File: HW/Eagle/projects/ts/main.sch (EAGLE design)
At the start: 46 parts, among them IC1 4050D, T1 IRFZ24N, T2 IRFZ24N, U1 ATMEGA328P-PU, U2 LM2576T, U3 HT7533, U4 LM75

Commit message: Minor HW changes
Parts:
- added H1: MOUNT-PAD-ROUND3.6, holes:MOUNT-PAD-ROUND3.6
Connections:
- net GND: now also H1.MOUNT
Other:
- moved on the sheet: LED1, R4, R9
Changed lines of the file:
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@@
 <part name="R13" library="rcl" deviceset="R-EU_" device="R0805" value="330R"/>
 <part name="LED1" library="led" deviceset="LED" device="5MM"/>
+<part name="H1" library="holes" deviceset="MOUNT-PAD-ROUND" device="3.6"/>
+<part name="GND11" library="supply1" deviceset="GND" device=""/>
 </parts>
 <sheets>
@@
 <instance part="+3V4" gate="G$1" x="246.888" y="88.9" rot="MR0"/>
 <instance part="GND13" gate="1" x="246.888" y="68.58" rot="MR0"/>
-<instance part="R4" gate="G$1" x="124.46" y="27.94"/>
+<instance part="R4" gate="G$1" x="134.62" y="27.94"/>
 <instance part="RESET" gate="1" x="220.98" y="114.3" rot="R270"/>
 <instance part="GND14" gate="1" x="213.36" y="106.68"/>
@@
 <instance part="R8" gate="G$1" x="21.336" y="35.56" rot="R180"/>
 <instance part="KEYPAD" gate="1" x="60.96" y="152.4"/>
-<instance part="R9" gate="G$1" x="104.14" y="15.24"/>
-<instance part="P+8" gate="VCC" x="97.79" y="19.05"/>
+<instance part="R9" gate="G$1" x="114.3" y="15.24"/>
+<instance part="P+8" gate="VCC" x="107.95" y="19.05"/>
 <instance part="T1" gate="G$1" x="38.1" y="124.46"/>
 <instance part="T2" gate="G$1" x="38.1" y="104.14"/>
@@
 <instance part="R12" gate="G$1" x="20.828" y="101.6" rot="R180"/>
 <instance part="R13" gate="G$1" x="20.828" y="121.92" rot="R180"/>
-<instance part="LED1" gate="G$1" x="114.3" y="15.24" rot="R90"/>
+<instance part="LED1" gate="G$1" x="124.46" y="15.24" rot="R90"/>
+<instance part="H1" gate="G$1" x="33.02" y="63.5"/>
+<instance part="GND11" gate="1" x="27.94" y="58.42"/>
 </instances>
 <busses>
@@
 <junction x="30.48" y="111.252"/>
 </segment>
+<segment>
+<pinref part="H1" gate="G$1" pin="MOUNT"/>
+<pinref part="GND11" gate="1" pin="GND"/>
+<wire x1="30.48" y1="63.5" x2="27.94" y2="63.5" width="0.1524" layer="91"/>
+<wire x1="27.94" y1="63.5" x2="27.94" y2="60.96" width="0.1524" layer="91"/>
+</segment>
 </net>
 <net name="VCC" class="0">
@@
 <pinref part="R9" gate="G$1" pin="1"/>
 <pinref part="P+8" gate="VCC" pin="VCC"/>
-<wire x1="99.06" y1="15.24" x2="97.79" y2="15.24" width="0.1524" layer="91"/>
-<wire x1="97.79" y1="15.24" x2="97.79" y2="16.51" width="0.1524" layer="91"/>
+<wire x1="109.22" y1="15.24" x2="107.95" y2="15.24" width="0.1524" layer="91"/>
+<wire x1="107.95" y1="15.24" x2="107.95" y2="16.51" width="0.1524" layer="91"/>
 </segment>
 </net>
@@
 <segment>
 <pinref part="R4" gate="G$1" pin="2"/>
-<wire x1="129.54" y1="27.94" x2="132.08" y2="27.94" width="0.1524" layer="91"/>
-<label x="132.08" y="27.94" size="1.778" layer="95" xref="yes"/>
+<wire x1="139.7" y1="27.94" x2="142.24" y2="27.94" width="0.1524" layer="91"/>
+<label x="142.24" y="27.94" size="1.778" layer="95" xref="yes"/>
 </segment>
 </net>
@@
 <segment>
 <pinref part="R4" gate="G$1" pin="1"/>
-<wire x1="119.38" y1="27.94" x2="116.84" y2="27.94" width="0.1524" layer="91"/>
-<label x="116.84" y="27.94" size="1.778" layer="95" rot="R180" xref="yes"/>
+<wire x1="129.54" y1="27.94" x2="127" y2="27.94" width="0.1524" layer="91"/>
+<label x="127" y="27.94" size="1.778" layer="95" rot="R180" xref="yes"/>
 </segment>
 <segment>
@@
 <net name="LED" class="0">
 <segment>
-<wire x1="119.38" y1="15.24" x2="124.46" y2="15.24" width="0.1524" layer="91"/>
-<label x="124.46" y="15.24" size="1.778" layer="95" xref="yes"/>
+<wire x1="129.54" y1="15.24" x2="134.62" y2="15.24" width="0.1524" layer="91"/>
+<label x="134.62" y="15.24" size="1.778" layer="95" xref="yes"/>
 <pinref part="LED1" gate="G$1" pin="C"/>
 </segment>
@@
 <segment>
 <pinref part="R9" gate="G$1" pin="2"/>
-<wire x1="109.22" y1="15.24" x2="111.76" y2="15.24" width="0.1524" layer="91"/>
+<wire x1="119.38" y1="15.24" x2="121.92" y2="15.24" width="0.1524" layer="91"/>
 <pinref part="LED1" gate="G$1" pin="A"/>
 </segment>

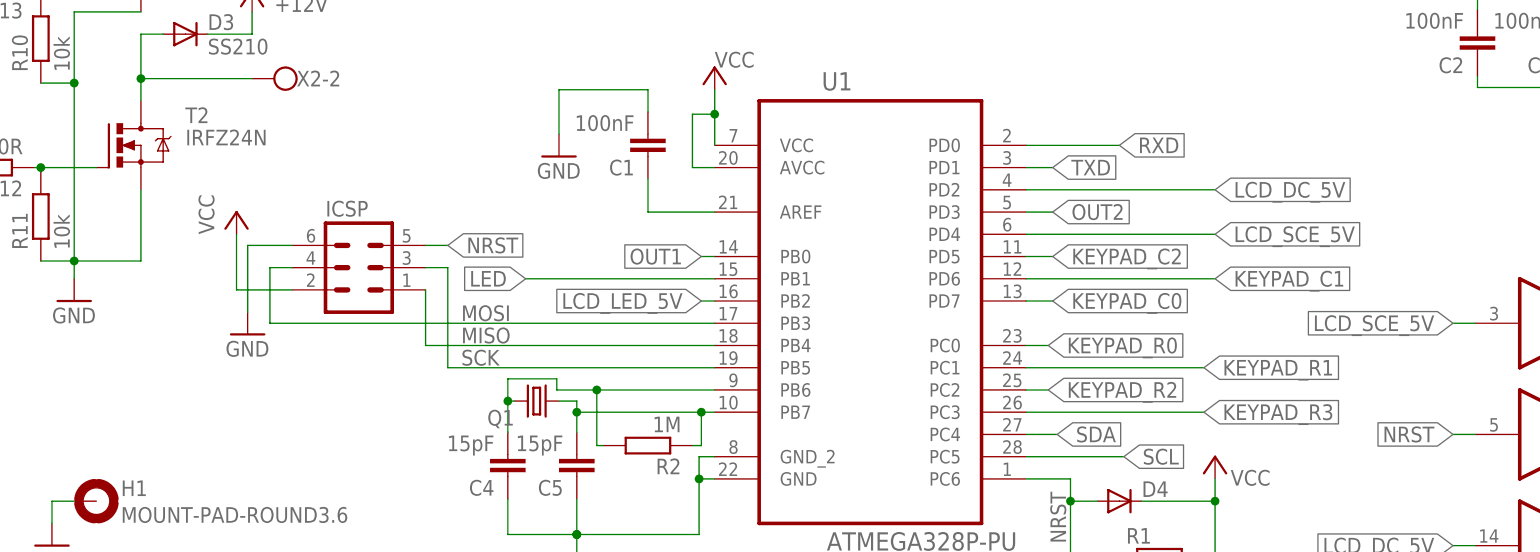
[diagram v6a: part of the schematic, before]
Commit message: Timer 1 is no longer used for PWM
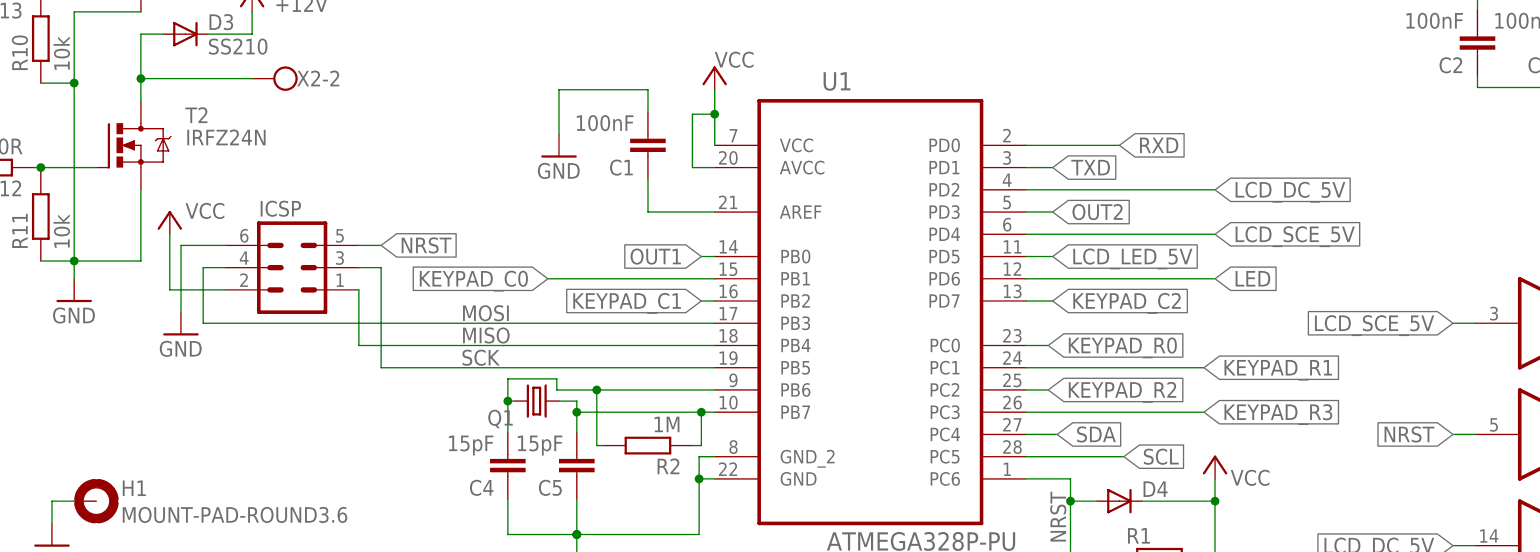
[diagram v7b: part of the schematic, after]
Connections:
- net KEYPAD_C0: now also U1.PB1; no longer U1.PD7
- net KEYPAD_C1: now also U1.PB2; no longer U1.PD6
- net KEYPAD_C2: now also U1.PD7; no longer U1.PD5
- net LCD_LED_5V: now also U1.PD5; no longer U1.PB2
- net LED: now also U1.PD6; no longer U1.PB1
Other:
- moved on the sheet: ICSP
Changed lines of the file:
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@@
 <instance part="R1" gate="G$1" x="154.432" y="57.15"/>
 <instance part="R2" gate="G$1" x="96.012" y="69.85" rot="R180"/>
-<instance part="ICSP" gate="1" x="62.992" y="90.17"/>
-<instance part="P+4" gate="VCC" x="49.022" y="96.52"/>
-<instance part="GND4" gate="1" x="50.292" y="82.55"/>
+<instance part="ICSP" gate="1" x="55.372" y="90.17"/>
+<instance part="P+4" gate="VCC" x="41.402" y="96.52" smashed="yes">
+<attribute name="VALUE" x="43.18" y="95.758" size="1.778" layer="96"/>
+</instance>
+<instance part="GND4" gate="1" x="42.672" y="82.55"/>
 <instance part="U2" gate="U" x="210.82" y="154.94"/>
 <instance part="FRAME1" gate="G$1" x="0" y="0"/>
@@
 <pinref part="ICSP" gate="1" pin="6"/>
 <pinref part="GND4" gate="1" pin="GND"/>
-<wire x1="55.372" y1="92.71" x2="50.292" y2="92.71" width="0.1524" layer="91"/>
-<wire x1="50.292" y1="92.71" x2="50.292" y2="85.09" width="0.1524" layer="91"/>
+<wire x1="47.752" y1="92.71" x2="42.672" y2="92.71" width="0.1524" layer="91"/>
+<wire x1="42.672" y1="92.71" x2="42.672" y2="85.09" width="0.1524" layer="91"/>
 </segment>
 <segment>
@@
 <pinref part="ICSP" gate="1" pin="2"/>
 <pinref part="P+4" gate="VCC" pin="VCC"/>
-<wire x1="55.372" y1="87.63" x2="49.022" y2="87.63" width="0.1524" layer="91"/>
-<wire x1="49.022" y1="87.63" x2="49.022" y2="93.98" width="0.1524" layer="91"/>
+<wire x1="47.752" y1="87.63" x2="41.402" y2="87.63" width="0.1524" layer="91"/>
+<wire x1="41.402" y1="87.63" x2="41.402" y2="93.98" width="0.1524" layer="91"/>
 </segment>
 <segment>
@@
 <segment>
 <pinref part="ICSP" gate="1" pin="1"/>
-<wire x1="103.632" y1="81.28" x2="70.612" y2="81.28" width="0.1524" layer="91"/>
-<wire x1="70.612" y1="81.28" x2="70.612" y2="87.63" width="0.1524" layer="91"/>
+<wire x1="103.632" y1="81.28" x2="62.992" y2="81.28" width="0.1524" layer="91"/>
+<wire x1="62.992" y1="81.28" x2="62.992" y2="87.63" width="0.1524" layer="91"/>
 <pinref part="U1" gate="A" pin="PB4"/>
 <label x="74.676" y="81.534" size="1.778" layer="95"/>
@@
 <segment>
 <pinref part="ICSP" gate="1" pin="5"/>
-<wire x1="70.612" y1="92.71" x2="73.152" y2="92.71" width="0.1524" layer="91"/>
-<label x="73.152" y="92.71" size="1.778" layer="95" xref="yes"/>
+<wire x1="62.992" y1="92.71" x2="65.532" y2="92.71" width="0.1524" layer="91"/>
+<label x="65.532" y="92.71" size="1.778" layer="95" xref="yes"/>
 </segment>
 <segment>
@@
 <segment>
 <pinref part="ICSP" gate="1" pin="4"/>
-<wire x1="52.832" y1="83.82" x2="52.832" y2="90.17" width="0.1524" layer="91"/>
-<wire x1="52.832" y1="90.17" x2="55.372" y2="90.17" width="0.1524" layer="91"/>
+<wire x1="45.212" y1="83.82" x2="45.212" y2="90.17" width="0.1524" layer="91"/>
+<wire x1="45.212" y1="90.17" x2="47.752" y2="90.17" width="0.1524" layer="91"/>
 <pinref part="U1" gate="A" pin="PB3"/>
-<wire x1="103.632" y1="83.82" x2="52.832" y2="83.82" width="0.1524" layer="91"/>
+<wire x1="103.632" y1="83.82" x2="45.212" y2="83.82" width="0.1524" layer="91"/>
 <label x="74.676" y="84.074" size="1.778" layer="95"/>
 </segment>
@@
 <net name="SCK" class="0">
 <segment>
-<wire x1="73.152" y1="78.74" x2="73.152" y2="90.17" width="0.1524" layer="91"/>
+<wire x1="65.532" y1="78.74" x2="65.532" y2="90.17" width="0.1524" layer="91"/>
 <pinref part="ICSP" gate="1" pin="3"/>
-<wire x1="73.152" y1="90.17" x2="70.612" y2="90.17" width="0.1524" layer="91"/>
+<wire x1="65.532" y1="90.17" x2="62.992" y2="90.17" width="0.1524" layer="91"/>
 <pinref part="U1" gate="A" pin="PB5"/>
-<wire x1="103.632" y1="78.74" x2="73.152" y2="78.74" width="0.1524" layer="91"/>
+<wire x1="103.632" y1="78.74" x2="65.532" y2="78.74" width="0.1524" layer="91"/>
 <label x="74.676" y="78.994" size="1.778" layer="95"/>
 </segment>
@@
 </segment>
 <segment>
-<pinref part="U1" gate="A" pin="PB2"/>
-<wire x1="103.632" y1="86.36" x2="102.108" y2="86.36" width="0.1524" layer="91"/>
-<label x="102.108" y="86.36" size="1.778" layer="95" rot="R180" xref="yes"/>
+<pinref part="U1" gate="A" pin="PD5"/>
+<wire x1="139.192" y1="91.44" x2="142.24" y2="91.44" width="0.1524" layer="91"/>
+<label x="142.24" y="91.44" size="1.778" layer="95" xref="yes"/>
 </segment>
 </net>
@@
 </segment>
 <segment>
-<pinref part="U1" gate="A" pin="PD5"/>
-<wire x1="139.192" y1="91.44" x2="142.24" y2="91.44" width="0.1524" layer="91"/>
-<label x="142.24" y="91.44" size="1.778" layer="95" xref="yes"/>
+<pinref part="U1" gate="A" pin="PD7"/>
+<wire x1="139.192" y1="86.36" x2="142.24" y2="86.36" width="0.1524" layer="91"/>
+<label x="142.24" y="86.36" size="1.778" layer="95" xref="yes"/>
 </segment>
 </net>
@@
 </segment>
 <segment>
+<pinref part="U1" gate="A" pin="PB2"/>
+<wire x1="103.632" y1="86.36" x2="102.108" y2="86.36" width="0.1524" layer="91"/>
+<label x="102.108" y="86.36" size="1.778" layer="95" rot="R180" xref="yes"/>
+</segment>
+</net>
+<net name="KEYPAD_C0" class="0">
+<segment>
+<pinref part="KEYPAD" gate="1" pin="1"/>
+<wire x1="68.58" y1="144.78" x2="88.9" y2="144.78" width="0.1524" layer="91"/>
+<label x="88.9" y="144.78" size="1.778" layer="95" xref="yes"/>
+</segment>
+<segment>
+<pinref part="U1" gate="A" pin="PB1"/>
+<wire x1="103.632" y1="88.9" x2="84.582" y2="88.9" width="0.1524" layer="91"/>
+<label x="84.582" y="88.9" size="1.778" layer="95" rot="R180" xref="yes"/>
+</segment>
+</net>
+<net name="OUT2" class="0">
+<segment>
+<pinref part="R12" gate="G$1" pin="2"/>
+<wire x1="15.748" y1="101.6" x2="14.732" y2="101.6" width="0.1524" layer="91"/>
+<label x="14.732" y="101.6" size="1.778" layer="95" rot="R180" xref="yes"/>
+</segment>
+<segment>
+<pinref part="U1" gate="A" pin="PD3"/>
+<wire x1="139.192" y1="96.52" x2="142.24" y2="96.52" width="0.1524" layer="91"/>
+<label x="142.24" y="96.52" size="1.778" layer="95" xref="yes"/>
+</segment>
+</net>
+<net name="LED" class="0">
+<segment>
+<wire x1="129.54" y1="15.24" x2="134.62" y2="15.24" width="0.1524" layer="91"/>
+<label x="134.62" y="15.24" size="1.778" layer="95" xref="yes"/>
+<pinref part="LED1" gate="G$1" pin="C"/>
+</segment>
+<segment>
 <pinref part="U1" gate="A" pin="PD6"/>
 <wire x1="139.192" y1="88.9" x2="160.782" y2="88.9" width="0.1524" layer="91"/>
@@
 </segment>
 </net>
-<net name="KEYPAD_C0" class="0">
-<segment>
-<pinref part="KEYPAD" gate="1" pin="1"/>
-<wire x1="68.58" y1="144.78" x2="88.9" y2="144.78" width="0.1524" layer="91"/>
-<label x="88.9" y="144.78" size="1.778" layer="95" xref="yes"/>
-</segment>
-<segment>
-<pinref part="U1" gate="A" pin="PD7"/>
-<wire x1="139.192" y1="86.36" x2="142.24" y2="86.36" width="0.1524" layer="91"/>
-<label x="142.24" y="86.36" size="1.778" layer="95" xref="yes"/>
-</segment>
-</net>
-<net name="OUT2" class="0">
-<segment>
-<pinref part="R12" gate="G$1" pin="2"/>
-<wire x1="15.748" y1="101.6" x2="14.732" y2="101.6" width="0.1524" layer="91"/>
-<label x="14.732" y="101.6" size="1.778" layer="95" rot="R180" xref="yes"/>
-</segment>
-<segment>
-<pinref part="U1" gate="A" pin="PD3"/>
-<wire x1="139.192" y1="96.52" x2="142.24" y2="96.52" width="0.1524" layer="91"/>
-<label x="142.24" y="96.52" size="1.778" layer="95" xref="yes"/>
-</segment>
-</net>
-<net name="LED" class="0">
-<segment>
-<wire x1="129.54" y1="15.24" x2="134.62" y2="15.24" width="0.1524" layer="91"/>
-<label x="134.62" y="15.24" size="1.778" layer="95" xref="yes"/>
-<pinref part="LED1" gate="G$1" pin="C"/>
-</segment>
-<segment>
-<pinref part="U1" gate="A" pin="PB1"/>
-<wire x1="103.632" y1="88.9" x2="82.042" y2="88.9" width="0.1524" layer="91"/>
-<label x="82.042" y="88.9" size="1.778" layer="95" rot="R180" xref="yes"/>
-</segment>
-</net>

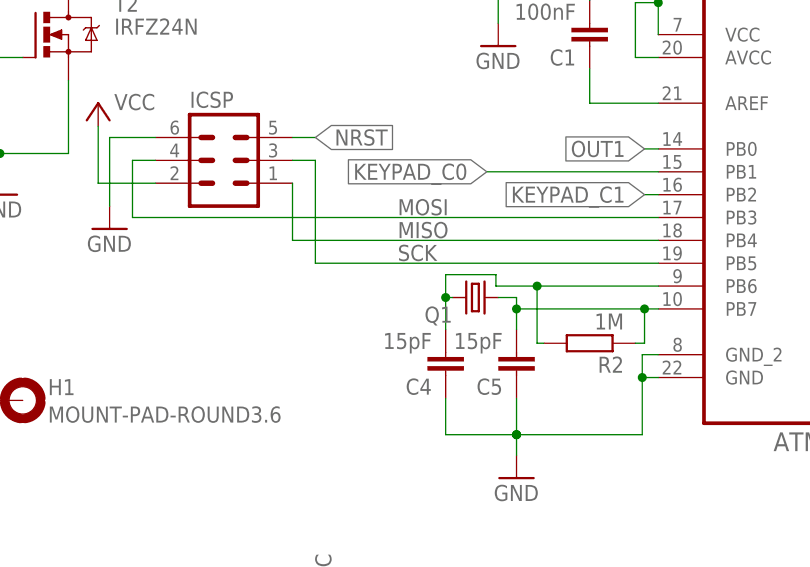
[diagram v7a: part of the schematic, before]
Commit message: Added value of crystal
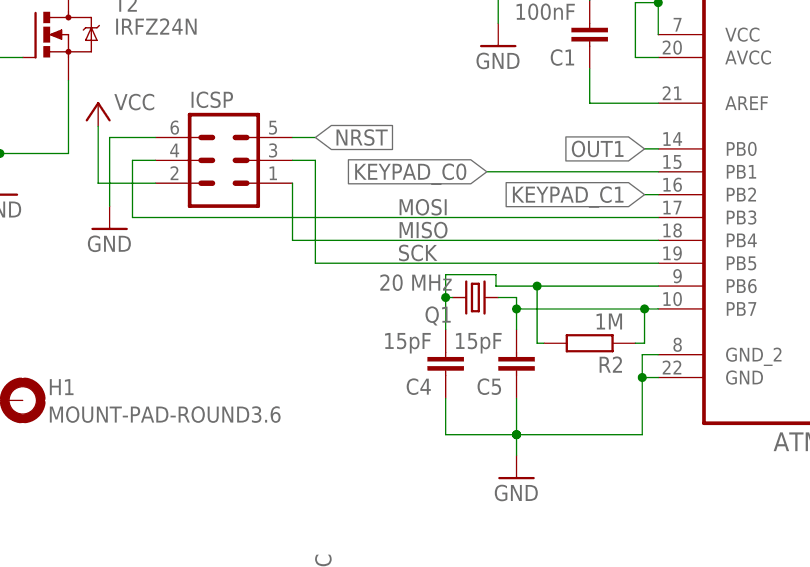
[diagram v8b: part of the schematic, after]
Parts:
- Q1: value (none) -> 20 MHz
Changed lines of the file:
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@@
 <part name="P+2" library="supply1" deviceset="VCC" device=""/>
 <part name="GND2" library="supply1" deviceset="GND" device=""/>
-<part name="Q1" library="crystal" deviceset="CRYSTAL" device="HC49S"/>
+<part name="Q1" library="crystal" deviceset="CRYSTAL" device="HC49S" value="20 MHz"/>
 <part name="C4" library="rcl" deviceset="C-EU" device="C0805" value="15pF"/>
 <part name="C5" library="rcl" deviceset="C-EU" device="C0805" value="15pF"/>
